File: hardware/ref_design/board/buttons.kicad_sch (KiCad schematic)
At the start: 16 parts, among them SW1 P1 UP, SW10 P2 DOWN, SW11 P2 LEFT, SW12 P2 RIGHT, SW13 P2 A, SW14 P2 B, SW15 P2 X, SW16 P2 Y, SW2 P1 DOWN, SW3 P1 LEFT, SW4 P1 RIGHT, SW5 P1 A, SW6 P1 B, SW7 P1 X, SW8 P1 Y, SW9 P2 UP

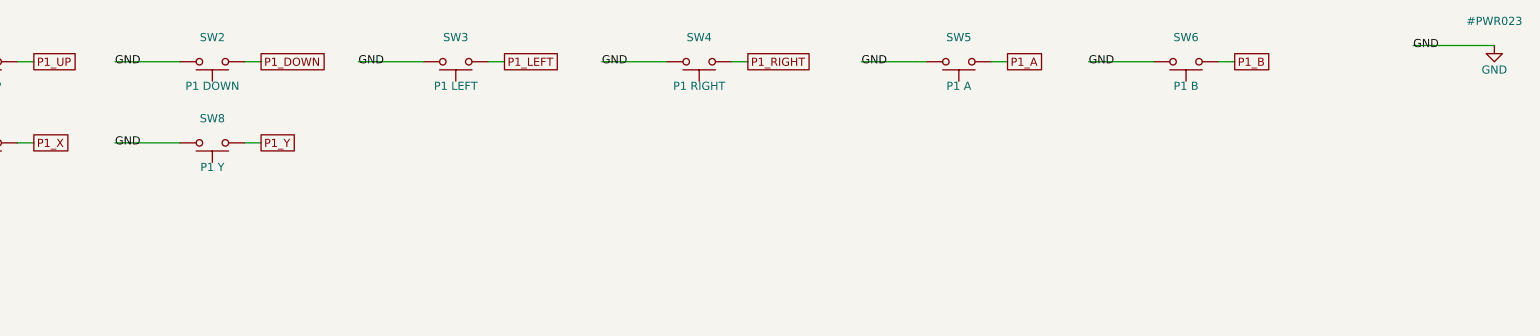
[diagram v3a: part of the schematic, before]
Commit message: 2-layer fork: approved circuit changes in the design data and schematic
TP4056 charger (500 mA, TEMP grounded) with USB load sharing (B5819W, AO3401A
gate fed through a BAT54WS so it switches at once on an unplug, 22 uF on VSYS),
ME6211 3V3 LDO on the power latch, RP2354B with its flash inside (only the
QSPI_SS strap outside), 27 ohm 0603 USB resistors, SRV05-4 ESD, PWM audio
through two RC poles into an FM8002A, seat 1's Y contact as the power button,
no LEDs, no thermistor. Thermal-via footprints use 0.3 mm holes. Netlist
check passes, ERC 0 errors.

Co-Authored-By: Claude Opus 5.5 <noreply@anthropic.com>
Claude-Session: https://claude.ai/code/session_01KGgEu3CbFtCsvHRQgAFiCN
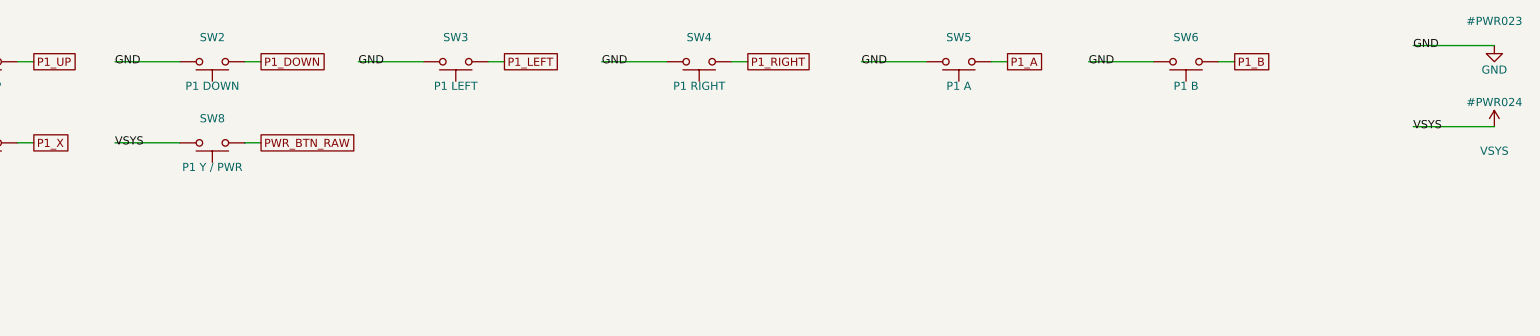
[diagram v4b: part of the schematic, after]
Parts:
- SW8: value P1 Y -> P1 Y / PWR
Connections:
- net GND: no longer SW8.2
- net P1_Y renamed PWR_BTN_RAW
- new net VSYS: SW8.2
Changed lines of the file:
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@@
       (xy 266.7 25.4))
+)
+  (wire
+    (pts
+      (xy 254 38.1)
+      (xy 266.7 38.1))
 )
   (text "Bare ENIG contacts (DSL_button_4ring) under DS Lite silicone; the firmware enables pull-ups."
@@
     (at 15.24 40.64 0)
 )
-  (label "GND"
+  (label "VSYS"
     (at 50.8 40.64 0)
 )
@@
     (at 254 25.4 0)
 )
+  (label "VSYS"
+    (at 254 38.1 0)
+)
   (global_label "P1_UP"
     (shape passive)
@@
     (at 38.1 40.64 0)
 )
-  (global_label "P1_Y"
+  (global_label "PWR_BTN_RAW"
     (shape passive)
     (at 73.66 40.64 0)
@@
         (font
           (size 1.27 1.27))))
-    (property "Value" "P1 Y"
+    (property "Value" "P1 Y / PWR"
       (at 66.04 44.45 0)
       (effects
@@
           (reference "#PWR023")
           (unit 1)))))
-)
+  (symbol
+    (lib_id "power:VCC")
+    (at 266.7 38.1 0)
+    (unit 1)
+    (in_bom yes)
+    (on_board yes)
+    (dnp no)
+    (property "Reference" "#PWR024"
+      (at 266.7 34.29 0)
+      (effects
+        (font
+          (size 1.27 1.27))))
+    (property "Value" "VSYS"
+      (at 266.7 41.91 0)
+      (effects
+        (font
+          (size 1.27 1.27))))
+    (property "Footprint" ""
+      (at 266.7 38.1 0)
+      (effects
+        (font
+          (size 1.27 1.27))
+        (hide yes)))
+    (property "Datasheet" ""
+      (at 266.7 38.1 0)
+      (effects
+        (font
+          (size 1.27 1.27))
+        (hide yes)))
+    (instances
+      (project ""
+        (path "/"
+          (reference "#PWR024")
+          (unit 1)))))
+)
